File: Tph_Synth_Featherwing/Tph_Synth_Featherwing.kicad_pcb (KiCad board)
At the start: 2 copper layers, 51 x 61.5 mm, 53 parts, among them J1 AudioJack3, J2 Conn_01x04, U1 PAM2401SCADJ, U2 LM2663M, U3 Opamp_Quad_Generic, U4 MCP4728

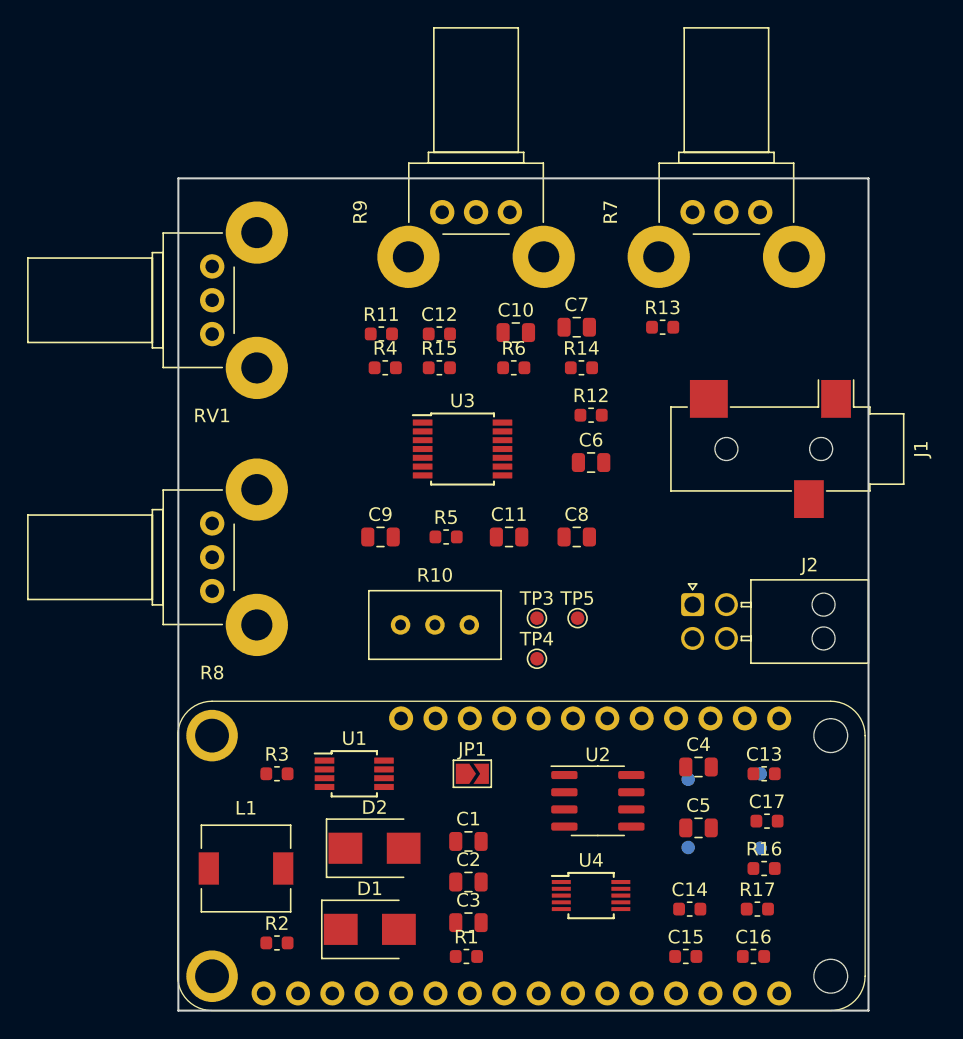
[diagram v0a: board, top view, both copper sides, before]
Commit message: Initial cut at part placement
Signed-off-by: Tisham Dhar <whatnickd@gmail.com>
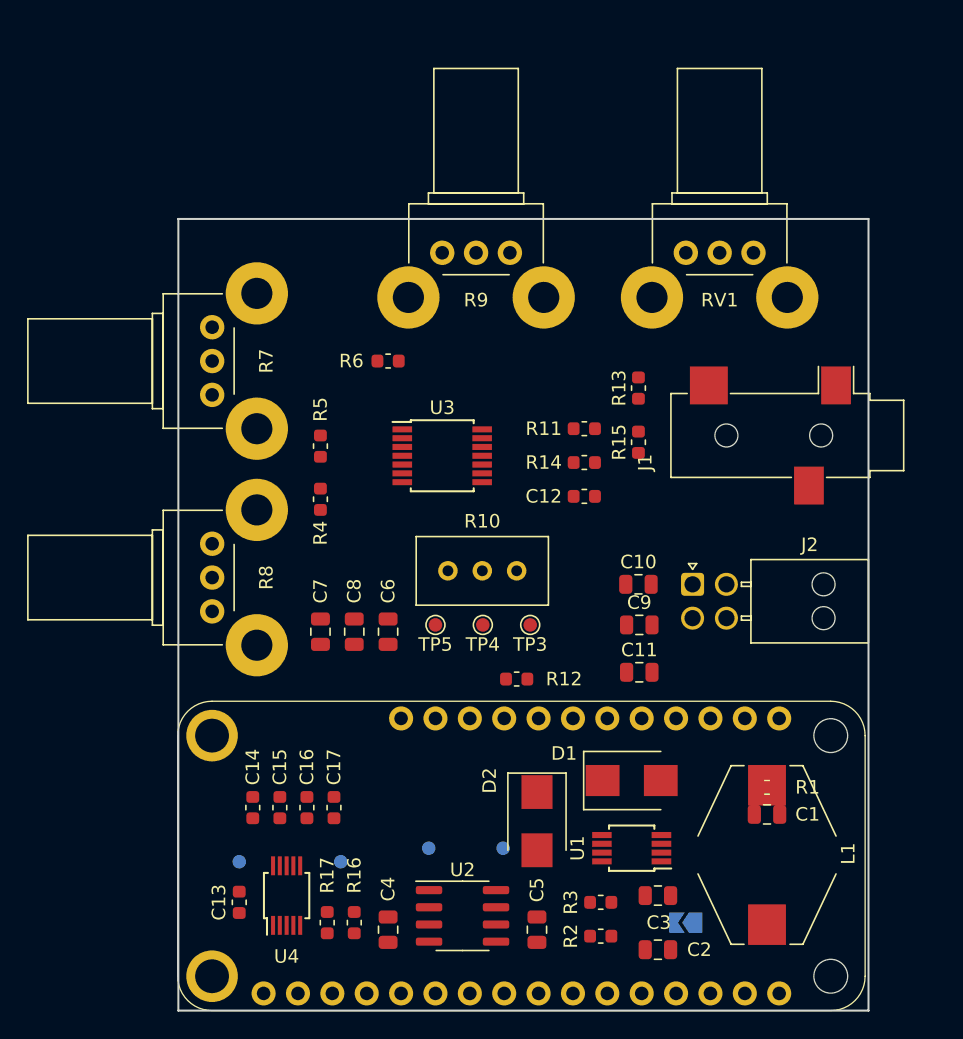
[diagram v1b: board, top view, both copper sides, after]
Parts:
- JP1: moved to B.Cu
- L1: footprint Inductor_SMD:L_6.3x6.3_H3 -> Inductor_SMD:L_Bourns-SRR1005
- moved R7 41.4 mm to (89.5, 86.0), turned to 180 degrees
- moved RV1 40.0 mm to (129.5, 80.5), turned to 90 degrees
- moved C13 39.9 mm to (91.5, 128.5), turned to 270 degrees
- moved TP6 39.0 mm to (91.5, 125.5)
- moved L1 38.5 mm to (130.5, 125.0), turned to 90 degrees
- moved C16 34.8 mm to (96.5, 121.5), turned to 90 degrees
- moved C14 33.1 mm to (92.5, 121.5), turned to 90 degrees
- moved C17 32.0 mm to (98.5, 121.5), turned to 90 degrees
- moved C15 32.0 mm to (94.5, 121.5), turned to 90 degrees
- moved R17 31.8 mm to (98.0, 130.0), turned to 90 degrees
- moved TP7 31.0 mm to (99.0, 125.5)
- moved R16 30.6 mm to (100.0, 130.0), turned to 90 degrees
- moved C7 29.4 mm to (97.5, 108.5), turned to 270 degrees
- moved C4 25.9 mm to (102.5, 130.5), turned to 270 degrees
- moved R3 25.7 mm to (118.2, 128.5), turned to 180 degrees
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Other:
- board size 51 x 61.5 mm -> 51 x 58.5 mm

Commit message: Pre-lim autoroute and renders
Signed-off-by: Tisham Dhar <whatnickd@gmail.com>
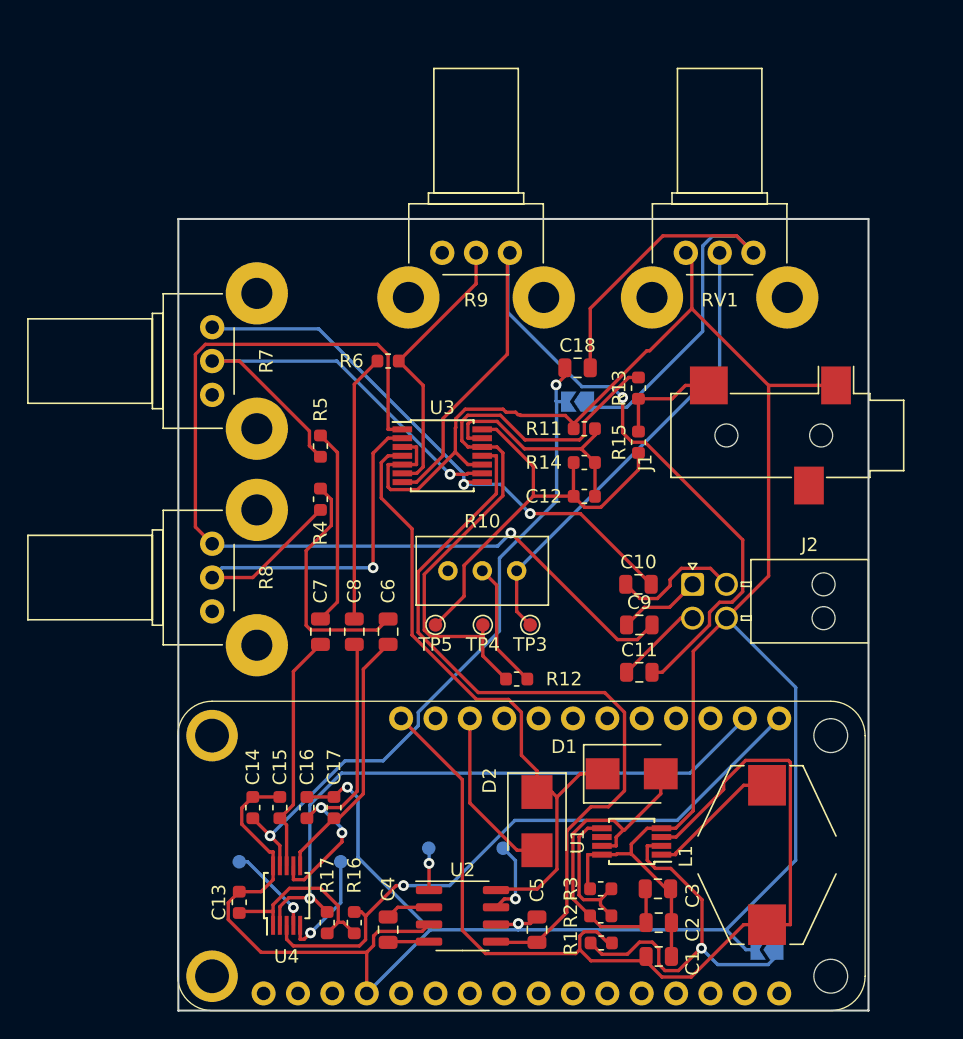
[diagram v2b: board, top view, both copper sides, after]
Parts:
- added C18: 10u, Capacitor_SMD:C_0805_2012Metric, F.Cu at (116.5, 89.0)
- added JP2: Jumper_2_Open, Jumper:SolderJumper-2_P1.3mm_Open_TrianglePad1.0x1.5mm, B.Cu at (116.5, 91.5)
- moved R1 16.8 mm to (118.2, 131.5)
- moved C1 13.2 mm to (122.5, 132.5), turned to 0 degrees
- moved JP1 6.32 mm to (130.5, 132.0)
- moved C2 2.00 mm to (122.5, 130.0)
- moved R2 1.50 mm to (118.2, 129.5)
- moved R3 1.00 mm to (118.2, 127.5)
- moved C3 0.50 mm to (122.4, 127.5)
- moved D1 0.50 mm to (120.5, 119.0)
- moved U1 0.50 mm to (120.5, 124.0)
- turned L1 to 270 degrees
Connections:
- RV1 pad 1: /Controlled Gain Output/IAC_in -> Net-(C18-Pad2)
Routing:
- net GND: track 0.00 -> 225.2 mm, vias 0 -> 2
- net /Boost_Converter/VBAT: track 0.00 -> 73.5 mm
- net Net-(C9-Pad2): track 0.00 -> 72.6 mm, vias 0 -> 1
- net Net-(C11-Pad2): track 0.00 -> 64.7 mm, vias 0 -> 1
- net /Controlled Gain Output/-5V: track 0.00 -> 57.7 mm
- net /Controlled Gain Output/IAC_in: track 0.00 -> 50.4 mm, vias 0 -> 2
- net /Controlled Gain Output/+5V: track 0.00 -> 48.5 mm
- net /Feathewing Headers/F_SCL: track 0.00 -> 47.3 mm, vias 0 -> 1
- net /Feathewing Headers/F_SDA: track 0.00 -> 46.6 mm, vias 0 -> 1
- net Net-(R12-Pad1): track 0.00 -> 46.1 mm
- net Net-(C10-Pad2): track 0.00 -> 42.2 mm, vias 0 -> 2
- net Net-(C18-Pad2): track 0.00 -> 41.1 mm
- net Net-(R5-Pad1): track 0.00 -> 35.0 mm, vias 0 -> 1
- net Net-(R10-Pad1): track 0.00 -> 34.1 mm
- net Net-(R4-Pad1): track 0.00 -> 33.3 mm, vias 0 -> 1
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
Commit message: More don't trust the autorouter
Signed-off-by: Tisham Dhar <whatnickd@gmail.com>
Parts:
- moved R9 30.8 mm to (89.5, 102.0), turned to 180 degrees
- moved R8 29.2 mm to (109.2, 80.5), turned to 90 degrees
- moved C1 14.0 mm to (116.8, 119.8), turned to 180 degrees
- moved R6 12.6 mm to (97.5, 100.0), turned to 270 degrees
- moved R1 12.3 mm to (121.8, 119.8), turned to 0 degrees
- moved D1 11.4 mm to (110.2, 124.0)
- moved R4 11.4 mm to (102.5, 88.5), turned to 180 degrees
- moved C14 7.50 mm to (96.2, 115.0), turned to 0 degrees
- moved D2 4.78 mm to (110.2, 119.0), turned to 0 degrees
- moved C15 4.29 mm to (96.2, 117.6), turned to 0 degrees
- moved R2 2.83 mm to (117.5, 132.2)
- moved C17 2.57 mm to (96.2, 122.8), turned to 0 degrees
- moved C2 2.00 mm to (122.5, 132.0)
- moved C16 1.36 mm to (96.2, 120.2), turned to 0 degrees
- moved R5 1.29 mm to (97.5, 93.5), turned to 270 degrees
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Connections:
- net Net-(C2-Pad1) renamed /Boost_Converter/BOOST_5V
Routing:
- net /Boost_Converter/VBAT: track 73.5 -> 37.9 mm, vias 0 -> 2
- net /Controlled Gain Output/IAC_in: track 50.4 -> 84.4 mm, vias 2 -> 1
- net Net-(C9-Pad2): track 72.6 -> 42.2 mm, vias 1 -> 2
- net Net-(C11-Pad2): track 64.7 -> 40.7 mm, vias 1 -> 2
- net GND: track 225.2 -> 244.5 mm, vias 2 -> 1
- net /Controlled Gain Output/VC_in: track 17.8 -> 35.9 mm, vias 0 -> 2
- net Net-(R6-Pad1): track 20.7 -> 37.5 mm, vias 0 -> 1
- net Net-(R4-Pad1): track 33.3 -> 16.5 mm, vias 1 -> 0
- net /Controlled Gain Output/-5V: track 57.7 -> 72.6 mm, vias 0 -> 2
- net Net-(C8-Pad1): track 19.8 -> 7.77 mm
- net Net-(JP1-Pad1): track 29.0 -> 17.7 mm
- net /Boost_Converter/VUSB: track 12.7 -> 6.46 mm
- net /Controlled Gain Output/VB_in: track 24.4 -> 18.8 mm, vias 2 -> 0
- net Net-(C18-Pad2): track 41.1 -> 36.2 mm
- net Net-(R10-Pad1): track 34.1 -> 38.4 mm
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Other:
- net class Power added: clearance 0.2, trace_width 0.4, via_dia 0.8, via_drill 0.4
